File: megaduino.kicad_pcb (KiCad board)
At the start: 2 copper layers, 48.9 x 52.7 mm, 48 parts, among them J1 Conn_01x20_Female, J2 Conn_01x20_Female, J3 Conn_01x13_Male, J4 Conn_01x10_Male, J5 Conn_01x10_Male, J6 Conn_01x10_Male, Q1 2N2219, Q2 2N2219, Q3 Q_NMOS_GDS, Q4 Q_NMOS_GDS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

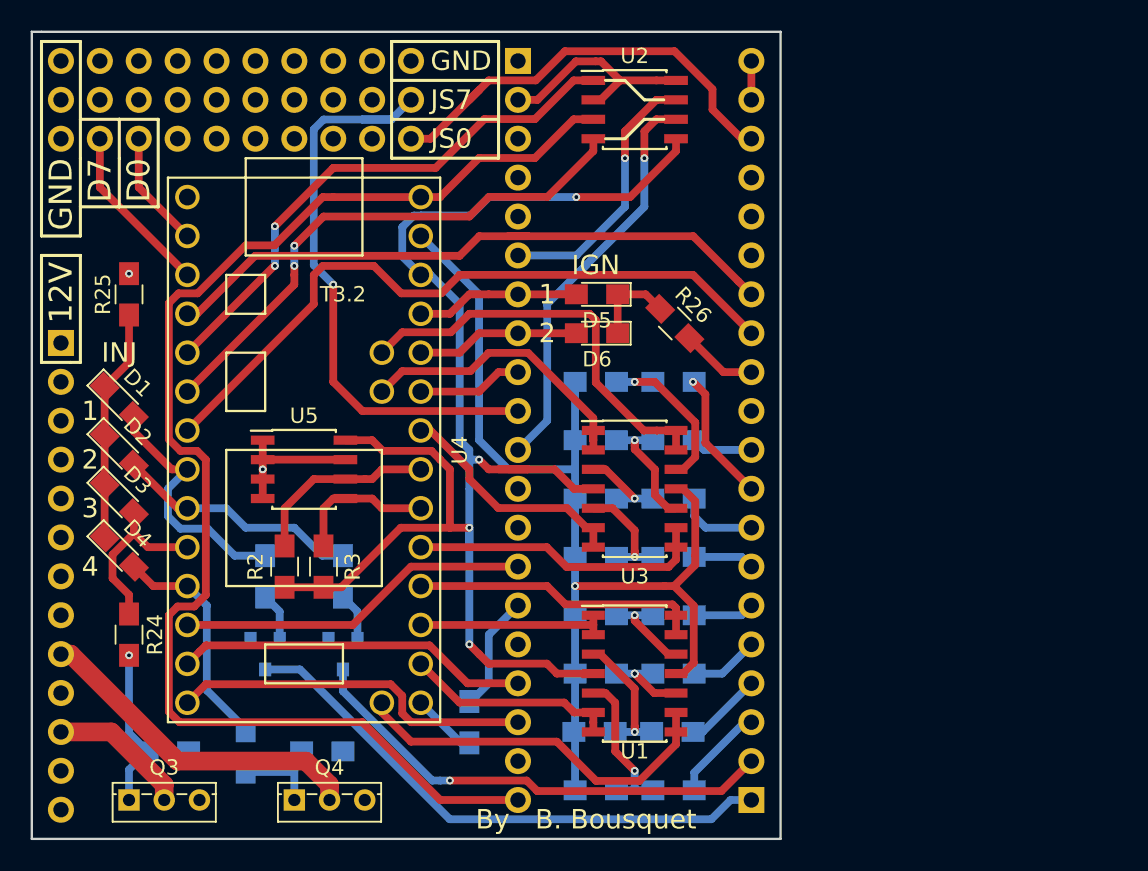
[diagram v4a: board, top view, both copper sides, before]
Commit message: remove components from under teensy
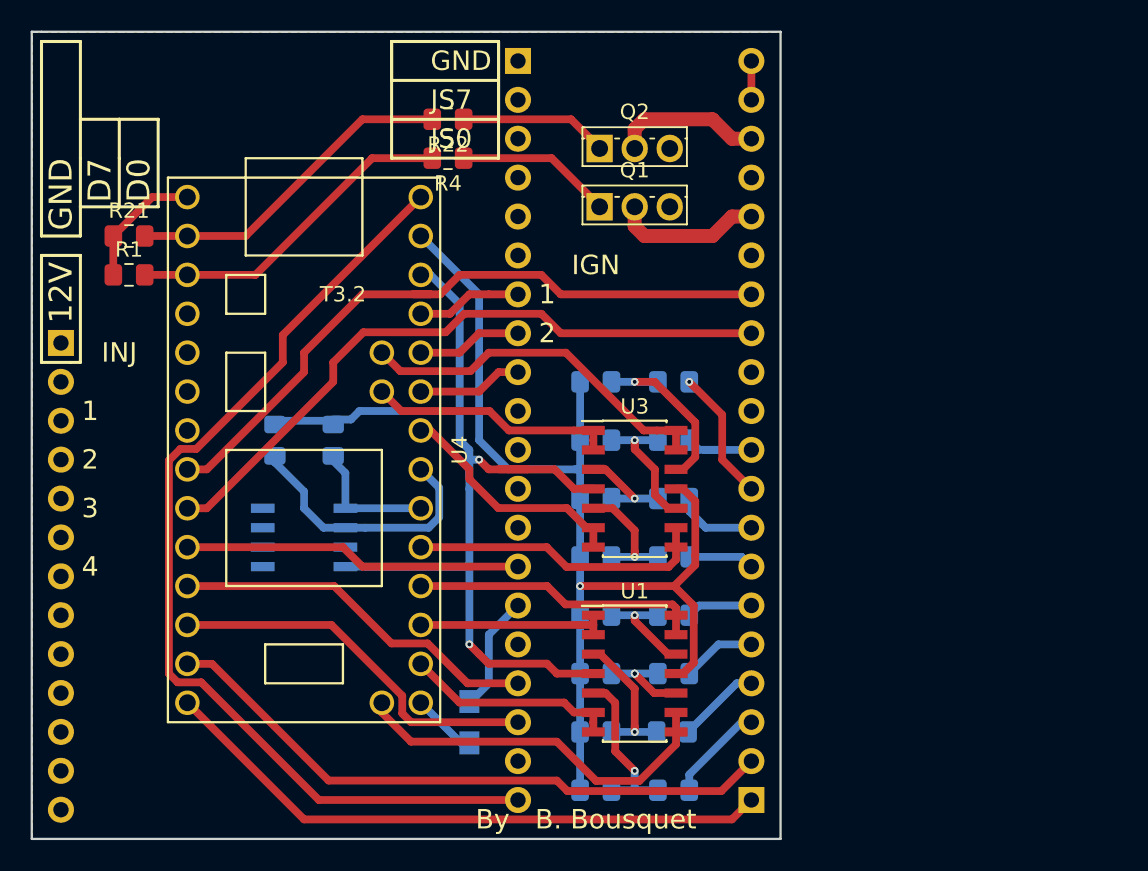
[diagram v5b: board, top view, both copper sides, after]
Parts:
- removed D1, D2, D3, D4, D5, D6: LED, LEDs:LED_0805_HandSoldering
- removed J4, J5, J6: Conn_01x10_Male, Pin_Headers:Pin_Header_Straight_1x10_Pitch2.54mm
- removed Q3, Q4: Q_NMOS_GDS, TO_SOT_Packages_THT:TO-251_IPAK_Vertical
- removed R23, R24: 1k, Resistors_SMD:R_0805_HandSoldering
- removed R25, R26: R, Resistors_SMD:R_0805_HandSoldering
- removed U2: MCP2562-E/P, Housings_SOIC:SOIC-8_3.9x4.9mm_Pitch1.27mm
- Q1, Q2: value 2N2219 -> RFD14N05L; footprint TO_SOT_Packages_SMD:SOT-23 -> Package_TO_SOT_THT:TO-251-3_Vertical; moved to F.Cu
- R1, R4: value 1k -> R; footprint Resistors_SMD:R_0805_HandSoldering -> Resistor_SMD:R_0805_2012Metric_Pad1.15x1.40mm_HandSolder; moved to F.Cu
- R10, R11, R12, R13, R14, R15, R16, R17, R18, R19, R20, R5, R6, R7, R8, R9: footprint Resistors_SMD:R_0805_HandSoldering -> Resistor_SMD:R_0805_2012Metric_Pad1.15x1.40mm_HandSolder
- R2, R3: footprint Resistors_SMD:R_0805_HandSoldering -> Resistor_SMD:R_0805_2012Metric_Pad1.15x1.40mm_HandSolder; moved to B.Cu
- R21, R22: value 100k -> R; footprint Resistors_SMD:R_0805_HandSoldering -> Resistor_SMD:R_0805_2012Metric_Pad1.15x1.40mm_HandSolder; moved to F.Cu
- U1, U3: footprint Housings_SOIC:SOIC-14_3.9x8.7mm_Pitch1.27mm -> Package_SO:SOIC-14_3.9x8.7mm_P1.27mm
- U5: footprint Housings_SOIC:SOIC-8_3.9x4.9mm_Pitch1.27mm -> Package_SO:SOIC-8_3.9x4.9mm_P1.27mm; moved to B.Cu
- moved R22 42.1 mm to (145.3, 72.4)
- moved Q2 37.0 mm to (155.2, 74.3), turned to 0 degrees
- moved Q1 36.5 mm to (155.2, 78.1), turned to 0 degrees
- moved R21 33.8 mm to (124.5, 80.0), turned to 0 degrees
- moved R4 28.2 mm to (145.3, 74.9), turned to 180 degrees
- moved R1 21.6 mm to (124.5, 82.5), turned to 0 degrees
- moved R2 8.28 mm to (134.0, 93.3), turned to 270 degrees
- moved R3 8.28 mm to (137.8, 93.3), turned to 270 degrees
- moved U5 4.44 mm to (135.9, 99.7)
- moved R6 0.08 mm to (154.9, 112.4)
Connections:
- J1 pad 10: JS7 -> (no net)
- J1 pad 11: CANL -> (no net)
- J1 pad 6: CANH -> (no net)
- J2 pad 1: Net-(J2-Pad1) -> INJ1
- J2 pad 16: (no net) -> JS2
- J2 pad 2: Net-(J2-Pad2) -> INJ2
- J3 pad 11: Net-(J3-Pad11) -> (no net)
- J3 pad 9: Net-(J3-Pad9) -> (no net)
- Q1 pad 1: Earth -> Net-(Q1-Pad1)
- Q1 pad 2: Net-(Q1-Pad2) -> JS2
- Q1 pad 3: Net-(J2-Pad1) -> Earth
- Q2 pad 1: Earth -> Net-(Q2-Pad1)
- Q2 pad 2: Net-(Q2-Pad2) -> JS0
- Q2 pad 3: Net-(J2-Pad2) -> Earth
- R1 pad 1: Net-(Q1-Pad2) -> Earth
- R1 pad 2: INJ1 -> INJ4
- R21 pad 2: Net-(Q3-Pad1) -> INJ3
- R22 pad 1: Earth -> Net-(Q2-Pad1)
- R22 pad 2: Net-(Q4-Pad1) -> INJ3
- R4 pad 1: Net-(Q2-Pad2) -> Net-(Q1-Pad1)
- R4 pad 2: INJ2 -> INJ4
- U4 pad 10: INJ3 -> IRQ0
- U4 pad 11: INJ4 -> IRQ1
- U4 pad 12: IRQ0 -> FAN
- U4 pad 13: IRQ1 -> INJ2
- U4 pad 14: FAN -> INJ1
- U4 pad 2: D0 -> INJ3
- U4 pad 3: D7 -> INJ4
- U4 pad 4: Idle -> (no net)
- U4 pad 5: Net-(U2-Pad1) -> (no net)
- U4 pad 6: Net-(U2-Pad4) -> (no net)
- U4 pad 7: FP -> (no net)
- U4 pad 8: INJ1 -> Idle
- U4 pad 9: INJ2 -> FP
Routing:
- net JS7: track 38.9 -> 0.00 mm, vias 1 -> 0
- net Net-(J2-Pad1): track 36.3 -> 0.00 mm
- net Net-(U2-Pad1): track 35.3 -> 0.00 mm, vias 2 -> 0
- net Net-(U2-Pad4): track 35.3 -> 0.00 mm, vias 2 -> 0
- net +3V3: track 97.6 -> 65.9 mm, vias 4 -> 2
- net Net-(J2-Pad2): track 31.6 -> 0.00 mm, vias 1 -> 0
- net CANL: track 27.5 -> 0.00 mm, vias 1 -> 0
- net INJ2: track 16.1 -> 41.1 mm
- net INJ1: track 16.5 -> 40.5 mm
- net +5V: track 87.8 -> 64.7 mm
- net Net-(J3-Pad9): track 22.1 -> 0.00 mm
- net Earth: track 28.3 -> 8.43 mm, vias 2 -> 0
- net JS0: track 28.6 -> 9.68 mm
- net CANH: track 17.4 -> 0.00 mm, vias 1 -> 0
- net Net-(D1-Pad1): track 15.7 -> 0.00 mm
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
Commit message: add inj3-4 drivers and CAN transceiver - no proto (yet?)
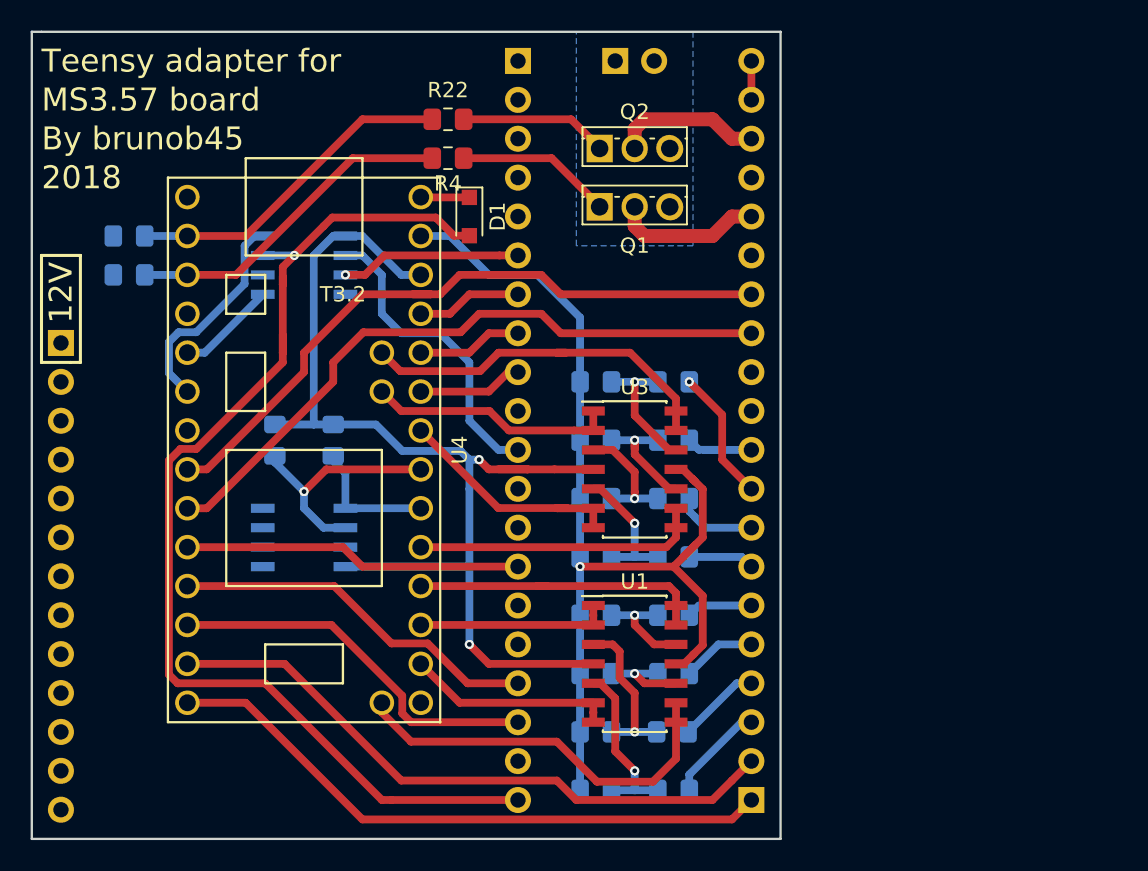
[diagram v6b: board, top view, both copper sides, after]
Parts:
- removed JP1: Jumper, Resistors_SMD:R_0805_HandSoldering
- added D1: D_Schottky, Diode_SMD:D_SOD-323_HandSoldering, F.Cu at (146.7, 78.7)
- added J4: Conn_01x02_Male, Connector_PinHeader_2.54mm:PinHeader_1x02_P2.54mm_Vertical, B.Cu at (156.2, 68.6)
- added U2: MCP2562-E-SN, Package_SO:SOIC-8_3.9x4.9mm_P1.27mm, B.Cu at (135.9, 81.9)
- R1, R21: value R -> 91k; moved to B.Cu
- R10, R12, R14, R16, R18, R20, R6, R8: value 330k -> 91k
- R11, R13, R15, R17, R19, R5, R7, R9: value 180k -> 49k
- R22, R4: value R -> 1k
- moved U3 1.27 mm to (157.5, 95.2)
- moved U1 0.63 mm to (157.5, 108.0)
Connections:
- J1 pad 11: (no net) -> CANL
- J1 pad 15: JS12 -> (no net)
- J1 pad 6: (no net) -> CANH
- U4 pad 20: Net-(JP1-Pad2) -> (no net)
- U4 pad 33: +5V -> Net-(D1-Pad1)
- U4 pad 5: (no net) -> Net-(U2-Pad1)
- U4 pad 6: (no net) -> Net-(U2-Pad4)
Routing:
- net CANL: track 0.00 -> 20.3 mm
- net Net-(U2-Pad4): track 0.00 -> 14.2 mm
- net CANH: track 0.00 -> 11.8 mm, vias 0 -> 1
- net +5V: track 64.7 -> 74.2 mm, vias 0 -> 1
- net Earth: track 8.43 -> 0.00 mm
- net JS12: track 7.63 -> 0.00 mm
- net Net-(U2-Pad1): track 0.00 -> 6.51 mm
- net +3V3: track 65.9 -> 72.3 mm
- net Net-(JP1-Pad2): track 4.26 -> 0.00 mm
- net Net-(R19-Pad2): track 11.9 -> 8.32 mm
- net Net-(D1-Pad1): track 0.00 -> 3.18 mm
- net GNDA: track 69.8 -> 67.7 mm
- net Net-(R2-Pad2): track 17.1 -> 15.3 mm, vias 0 -> 1
- net Net-(R15-Pad2): track 5.87 -> 7.41 mm
- net A2: track 24.8 -> 26.0 mm
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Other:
- net class Default: trace_width 0.254 -> 0.508; via_dia 0.508 -> 0.6096; via_drill 0.254 -> 0.3048
- board text added: "2018"
- board text added: "By brunob45"
- board text added: "MS3.57 board"
- board text added: "Teensy adapter for"
- board text removed: "1"
- board text removed: "2"
- board text removed: "3"
- board text removed: "4"
- board text removed: "By B. Bousquet"
- board text removed: "D0"
- board text removed: "D7"
- board text removed: "GND"
- board text removed: "IGN"
- board text removed: "INJ"
- board text removed: "JS0"
- board text removed: "JS7"

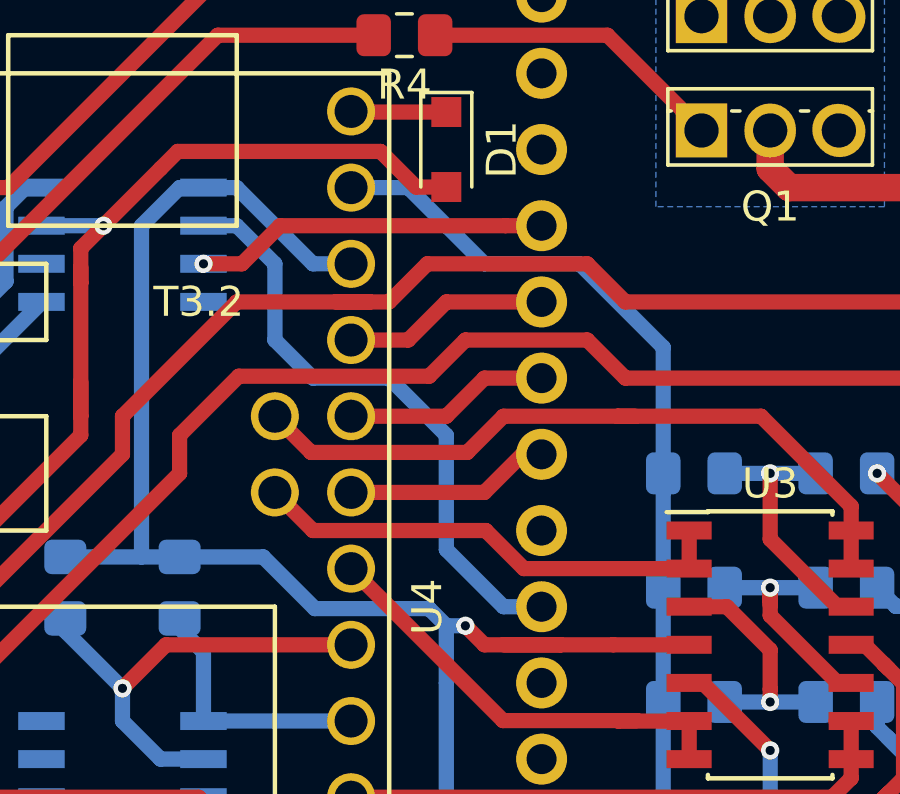
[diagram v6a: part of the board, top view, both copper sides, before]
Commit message: add 120R resistor for CAN
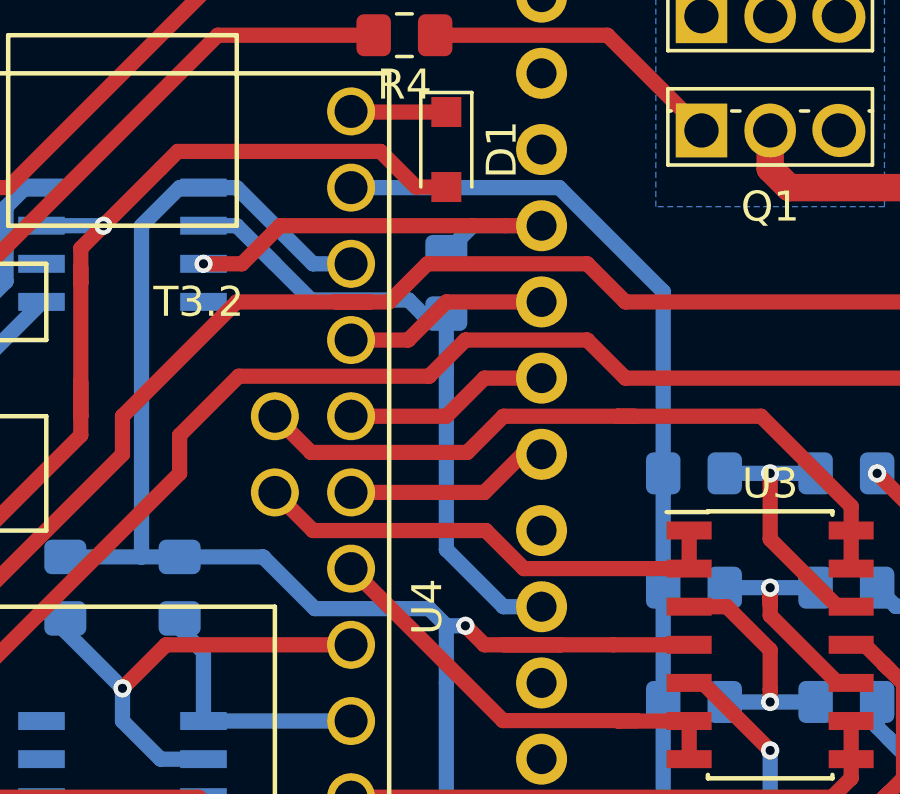
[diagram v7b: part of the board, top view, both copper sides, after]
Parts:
- added R23: 120, Resistor_SMD:R_0805_2012Metric_Pad1.15x1.40mm_HandSolder, B.Cu at (146.7, 83.2)
- J3: footprint Pin_Headers:Pin_Header_Straight_1x13_Pitch2.54mm -> Connector_PinHeader_2.54mm:PinHeader_1x13_P2.54mm_Vertical
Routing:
- net CANH: track 11.8 -> 15.3 mm
- net CANL: track 20.3 -> 22.0 mm
- net GNDA: track 67.7 -> 68.8 mm

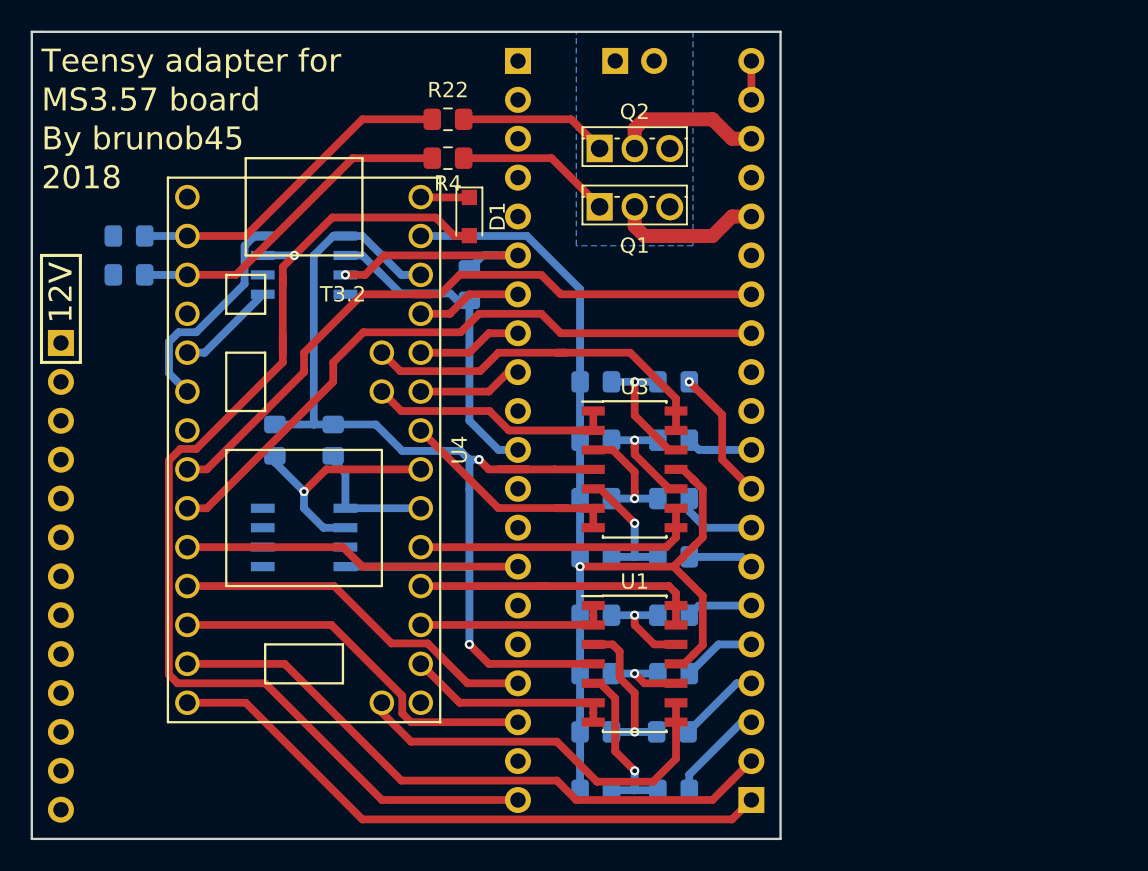
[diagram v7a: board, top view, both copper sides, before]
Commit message: add Serial-BT HC-06 connection
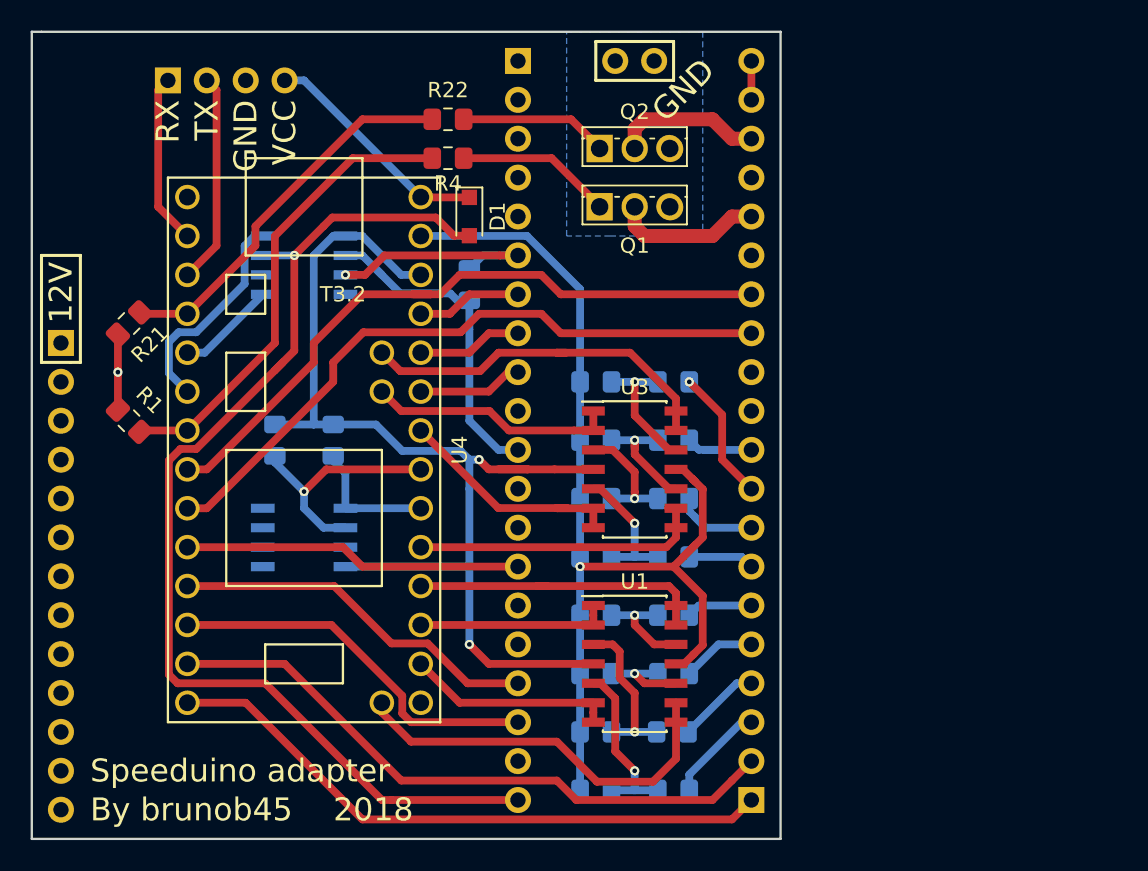
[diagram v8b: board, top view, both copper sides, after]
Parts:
- added J5: Conn_01x04_Male, Connector_PinHeader_2.54mm:PinHeader_1x04_P2.54mm_Vertical, B.Cu at (127.0, 69.8)
- R1, R21: moved to F.Cu
- moved R1 9.53 mm to (124.5, 92.1), turned to 315 degrees
- moved R21 5.71 mm to (124.5, 85.7), turned to 45 degrees
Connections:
- U4 pad 2: INJ3 -> Net-(J5-Pad1)
- U4 pad 3: INJ4 -> Net-(J5-Pad2)
- U4 pad 4: (no net) -> INJ3
- U4 pad 7: (no net) -> INJ4
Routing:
- net Net-(J5-Pad2): track 0.00 -> 13.8 mm
- net Net-(D1-Pad1): track 3.18 -> 15.2 mm
- net Net-(J5-Pad1): track 0.00 -> 11.2 mm
- net INJ4: track 21.9 -> 30.2 mm
- net Earth: track 0.00 -> 4.90 mm, vias 0 -> 1
- net INJ3: track 21.9 -> 24.8 mm
- net +5V: track 74.2 -> 73.3 mm
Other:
- board text added: "GND"
- board text added: "RX"
- board text added: "Speeduino adapter"
- board text added: "TX"
- board text added: "VCC"
- board text removed: "MS3.57 board"
- board text removed: "Teensy adapter for"
